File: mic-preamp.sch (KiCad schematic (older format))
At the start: 11 parts, among them J1 Conn_01x07_Female, J2 Conn_01x04_Female, U1 LM358

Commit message: gg
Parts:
- removed unit 1 of U1
- added unit 2 of U1
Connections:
- net +2V5: now also U1.5 (+IN)
- net GND: now also J2.3 (Pin_3); no longer J2.4 (Pin_4)
- net MICOUT: now also J2.4 (Pin_4), U1.7 (OUT); no longer J2.2 (Pin_2)
- net PTT: now also J2.2 (Pin_2); no longer J2.3 (Pin_3)
- net at C3.2, R4.2, R5.1: now also U1.6 (-IN)
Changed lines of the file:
@@
-$Comp
-L Xenir:LM358 U1
-U 1 1 639381F3
-P 3925 4025
-F 0 "U1" H 3875 4050 70  0000 C CNN
-F 1 "LM358" H 4000 3825 70  0000 C CNN
-F 2 "Xenir:SOIC8" H 3875 3975 50  0001 C CNN
-F 3 "" H 3875 3975 50  0001 C CNN
-	1    3925 4025
-	1    0    0    -1
-$EndComp
 $Comp
 L Xenir:LM358 U1
@@
 Text GLabel 5500 3675 0    50   Input ~ 0
 FREQUPDN
-Text GLabel 5500 4650 0    50   Input ~ 0
+Text GLabel 5500 4550 0    50   Input ~ 0
 PTT
-Text GLabel 5500 4550 0    50   Input ~ 0
+Text GLabel 5500 4750 0    50   Input ~ 0
 MICOUT
 Text GLabel 2025 4125 0    50   Input ~ 0
@@
 Wire Wire Line
 	4325 4025 4225 4025
-Connection ~ 4225 4025
 $Comp
 L power:GND #PWR0108
 U 1 1 63989072
-P 5500 4750
-F 0 "#PWR0108" H 5500 4500 50  0001 C CNN
-F 1 "GND" H 5505 4577 50  0000 C CNN
-F 2 "" H 5500 4750 50  0001 C CNN
-F 3 "" H 5500 4750 50  0001 C CNN
-	1    5500 4750
+P 4900 4650
+F 0 "#PWR0108" H 4900 4400 50  0001 C CNN
+F 1 "GND" H 4905 4477 50  0000 C CNN
+F 2 "" H 4900 4650 50  0001 C CNN
+F 3 "" H 4900 4650 50  0001 C CNN
+	1    4900 4650
 	1    0    0    -1
 $EndComp
@@
 Wire Wire Line
 	2175 4125 2025 4125
+Wire Wire Line
+	5500 4650 4900 4650
+$Comp
+L Xenir:LM358 U1
+U 2 1 6387C712
+P 3925 4025
+F 0 "U1" H 3775 3975 70  0000 L BNN
+F 1 "LM358" H 3875 4275 70  0000 L BNN
+F 2 "" H 3875 3975 50  0001 C CNN
+F 3 "" H 3875 3975 50  0001 C CNN
+	2    3925 4025
+	1    0    0    -1
+$EndComp
+Connection ~ 4225 4025
 $EndSCHEMATC

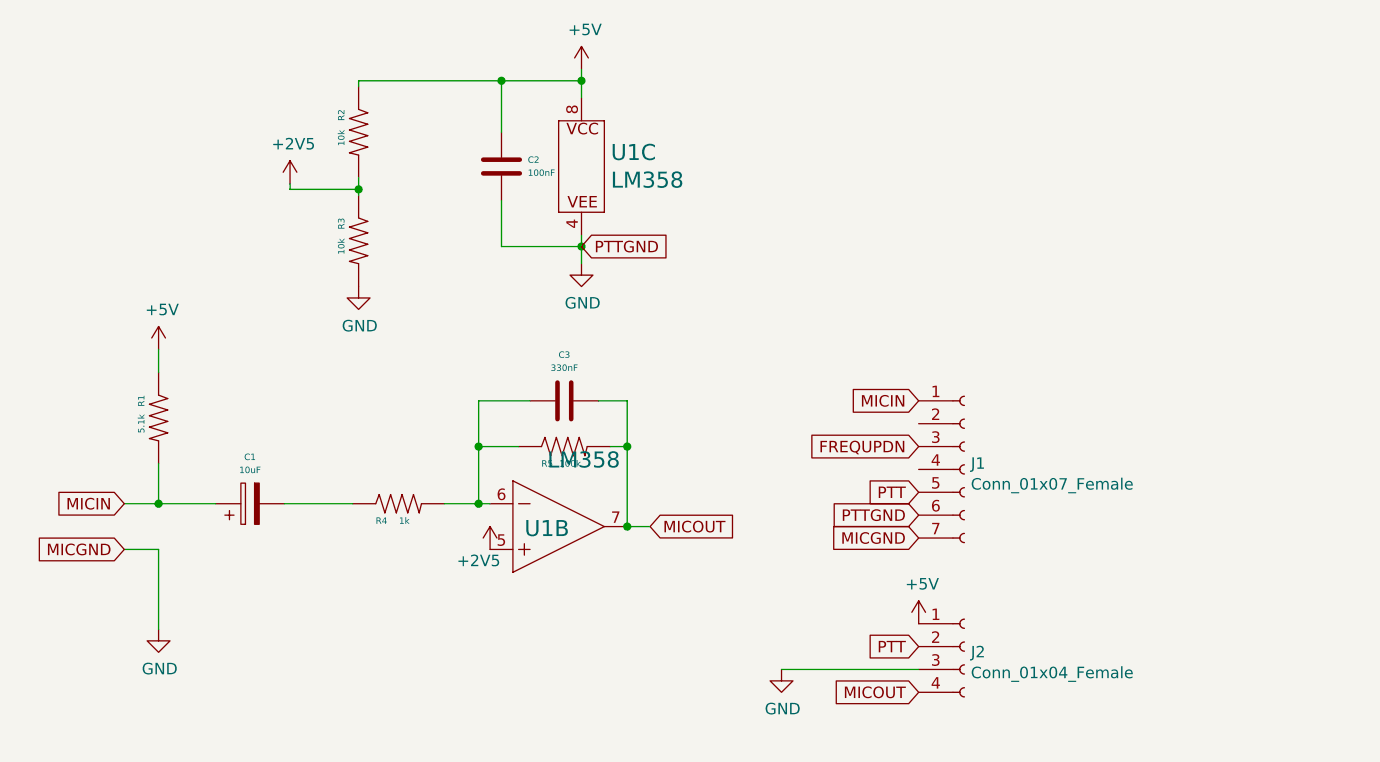
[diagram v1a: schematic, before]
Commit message: added output cap
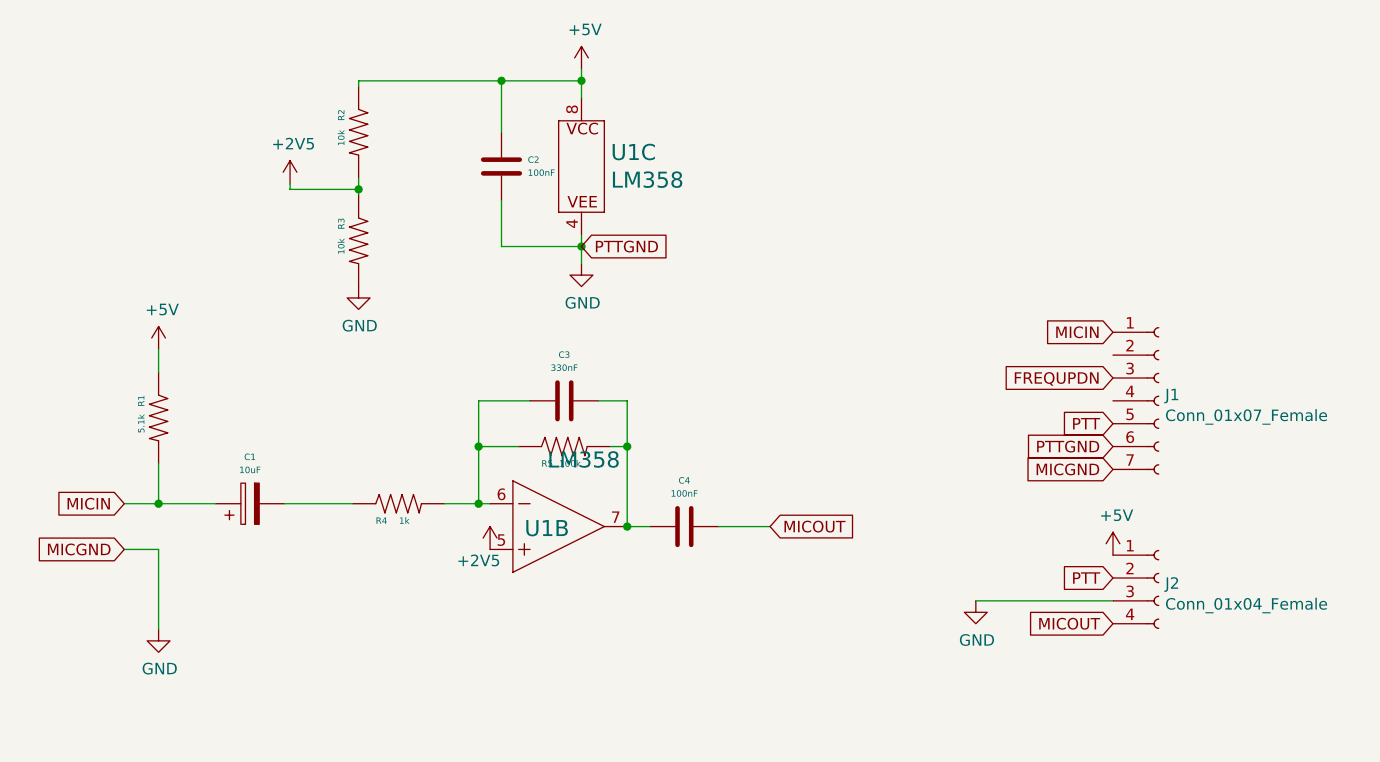
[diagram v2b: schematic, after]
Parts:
- added C4: 100nF, Xenir:Capacitor 1206, symbol Xenir:Capacitor
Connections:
- net MICOUT: now also C4.1; no longer C3.1, R5.2, U1.7 (OUT)
- new net: C3.1, C4.2, R5.2, U1.7 (OUT)
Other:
- moved on the sheet: J1, J2
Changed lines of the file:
@@
 L Connector:Conn_01x07_Female J1
 U 1 1 63973E4A
-P 5700 3775
-F 0 "J1" H 5728 3801 50  0000 L CNN
-F 1 "Conn_01x07_Female" H 5728 3710 50  0000 L CNN
-F 2 "Connector_PinHeader_2.54mm:PinHeader_1x07_P2.54mm_Vertical" H 5700 3775 50  0001 C CNN
-F 3 "~" H 5700 3775 50  0001 C CNN
-	1    5700 3775
+P 6550 3475
+F 0 "J1" H 6578 3501 50  0000 L CNN
+F 1 "Conn_01x07_Female" H 6578 3410 50  0000 L CNN
+F 2 "Connector_PinHeader_2.54mm:PinHeader_1x07_P2.54mm_Vertical" H 6550 3475 50  0001 C CNN
+F 3 "~" H 6550 3475 50  0001 C CNN
+	1    6550 3475
 	1    0    0    -1
 $EndComp
-Text GLabel 5500 4075 0    50   Input ~ 0
+Text GLabel 6350 3775 0    50   Input ~ 0
 MICGND
-Text GLabel 5500 3975 0    50   Input ~ 0
+Text GLabel 6350 3675 0    50   Input ~ 0
 PTTGND
-Text GLabel 5500 3875 0    50   Input ~ 0
+Text GLabel 6350 3575 0    50   Input ~ 0
 PTT
-Text GLabel 5500 3475 0    50   Input ~ 0
+Text GLabel 6350 3175 0    50   Input ~ 0
 MICIN
-Text GLabel 5500 3675 0    50   Input ~ 0
+Text GLabel 6350 3375 0    50   Input ~ 0
 FREQUPDN
-Text GLabel 5500 4550 0    50   Input ~ 0
+Text GLabel 6350 4250 0    50   Input ~ 0
 PTT
-Text GLabel 5500 4750 0    50   Input ~ 0
+Text GLabel 6350 4450 0    50   Input ~ 0
 MICOUT
 Text GLabel 2025 4125 0    50   Input ~ 0
@@
 Text GLabel 4025 2800 2    50   Input ~ 0
 PTTGND
-Text GLabel 4325 4025 2    50   Input ~ 0
+Text GLabel 4850 4025 2    50   Input ~ 0
 MICOUT
-Wire Wire Line
-	4325 4025 4225 4025
 $Comp
 L power:GND #PWR0108
 U 1 1 63989072
-P 4900 4650
-F 0 "#PWR0108" H 4900 4400 50  0001 C CNN
-F 1 "GND" H 4905 4477 50  0000 C CNN
-F 2 "" H 4900 4650 50  0001 C CNN
-F 3 "" H 4900 4650 50  0001 C CNN
-	1    4900 4650
+P 5750 4350
+F 0 "#PWR0108" H 5750 4100 50  0001 C CNN
+F 1 "GND" H 5755 4177 50  0000 C CNN
+F 2 "" H 5750 4350 50  0001 C CNN
+F 3 "" H 5750 4350 50  0001 C CNN
+	1    5750 4350
 	1    0    0    -1
 $EndComp
@@
 L Connector:Conn_01x04_Female J2
 U 1 1 6398BACA
-P 5700 4550
-F 0 "J2" H 5728 4526 50  0000 L CNN
-F 1 "Conn_01x04_Female" H 5728 4435 50  0000 L CNN
-F 2 "Connector_PinHeader_2.54mm:PinHeader_1x04_P2.54mm_Vertical" H 5700 4550 50  0001 C CNN
-F 3 "~" H 5700 4550 50  0001 C CNN
-	1    5700 4550
+P 6550 4250
+F 0 "J2" H 6578 4226 50  0000 L CNN
+F 1 "Conn_01x04_Female" H 6578 4135 50  0000 L CNN
+F 2 "Connector_PinHeader_2.54mm:PinHeader_1x04_P2.54mm_Vertical" H 6550 4250 50  0001 C CNN
+F 3 "~" H 6550 4250 50  0001 C CNN
+	1    6550 4250
 	1    0    0    -1
 $EndComp
@@
 L power:+5V #PWR0109
 U 1 1 63993EEF
-P 5500 4450
-F 0 "#PWR0109" H 5500 4300 50  0001 C CNN
-F 1 "+5V" H 5515 4623 50  0000 C CNN
-F 2 "" H 5500 4450 50  0001 C CNN
-F 3 "" H 5500 4450 50  0001 C CNN
-	1    5500 4450
+P 6350 4150
+F 0 "#PWR0109" H 6350 4000 50  0001 C CNN
+F 1 "+5V" H 6365 4323 50  0000 C CNN
+F 2 "" H 6350 4150 50  0001 C CNN
+F 3 "" H 6350 4150 50  0001 C CNN
+	1    6350 4150
 	1    0    0    -1
 $EndComp
@@
 	2175 4125 2025 4125
 Wire Wire Line
-	5500 4650 4900 4650
+	6350 4350 5750 4350
 $Comp
 L Xenir:LM358 U1
@@
 	1    0    0    -1
 $EndComp
+$Comp
+L Xenir:Capacitor C4
+U 1 1 638A53E8
+P 4475 4025
+F 0 "C4" H 4475 3824 28  0000 C CNN
+F 1 "100nF" H 4475 3881 28  0000 C CNN
+F 2 "Xenir:Capacitor 1206" H 4475 3875 50  0001 C CNN
+F 3 "" H 4475 3875 50  0001 C CNN
+	1    4475 4025
+	-1   0    0    1
+$EndComp
+Wire Wire Line
+	4225 4025 4325 4025
 Connection ~ 4225 4025
+Wire Wire Line
+	4625 4025 4850 4025
 $EndSCHEMATC

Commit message: 330pF
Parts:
- C3: value 330nF -> 330pF
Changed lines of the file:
@@
 P 3950 3475
 F 0 "C3" H 3950 3274 28  0000 C CNN
-F 1 "330nF" H 3950 3331 28  0000 C CNN
+F 1 "330pF" H 3950 3331 28  0000 C CNN
 F 2 "Xenir:Capacitor 1206" H 3950 3325 50  0001 C CNN
 F 3 "" H 3950 3325 50  0001 C CNN
@@
 P 3925 4025
 F 0 "U1" H 3775 3975 70  0000 L BNN
-F 1 "LM358" H 3875 4275 70  0000 L BNN
+F 1 "LM358" H 3900 3800 70  0000 L BNN
 F 2 "" H 3875 3975 50  0001 C CNN
 F 3 "" H 3875 3975 50  0001 C CNN
